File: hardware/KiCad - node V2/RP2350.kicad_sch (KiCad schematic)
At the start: 87 parts, among them J3 USB_C_Receptacle_USB2.0_14P, SW1 BOOTSEL, U1 RP2350A, U2 THVD1450D, U3 ADXL355BEZ, U4 TPS2121RUXR, U5 USBLC6-2SC6, U6 TLV75733PDBV, U7 W25Q128JVS, U8 TPS7A20xxxDBV

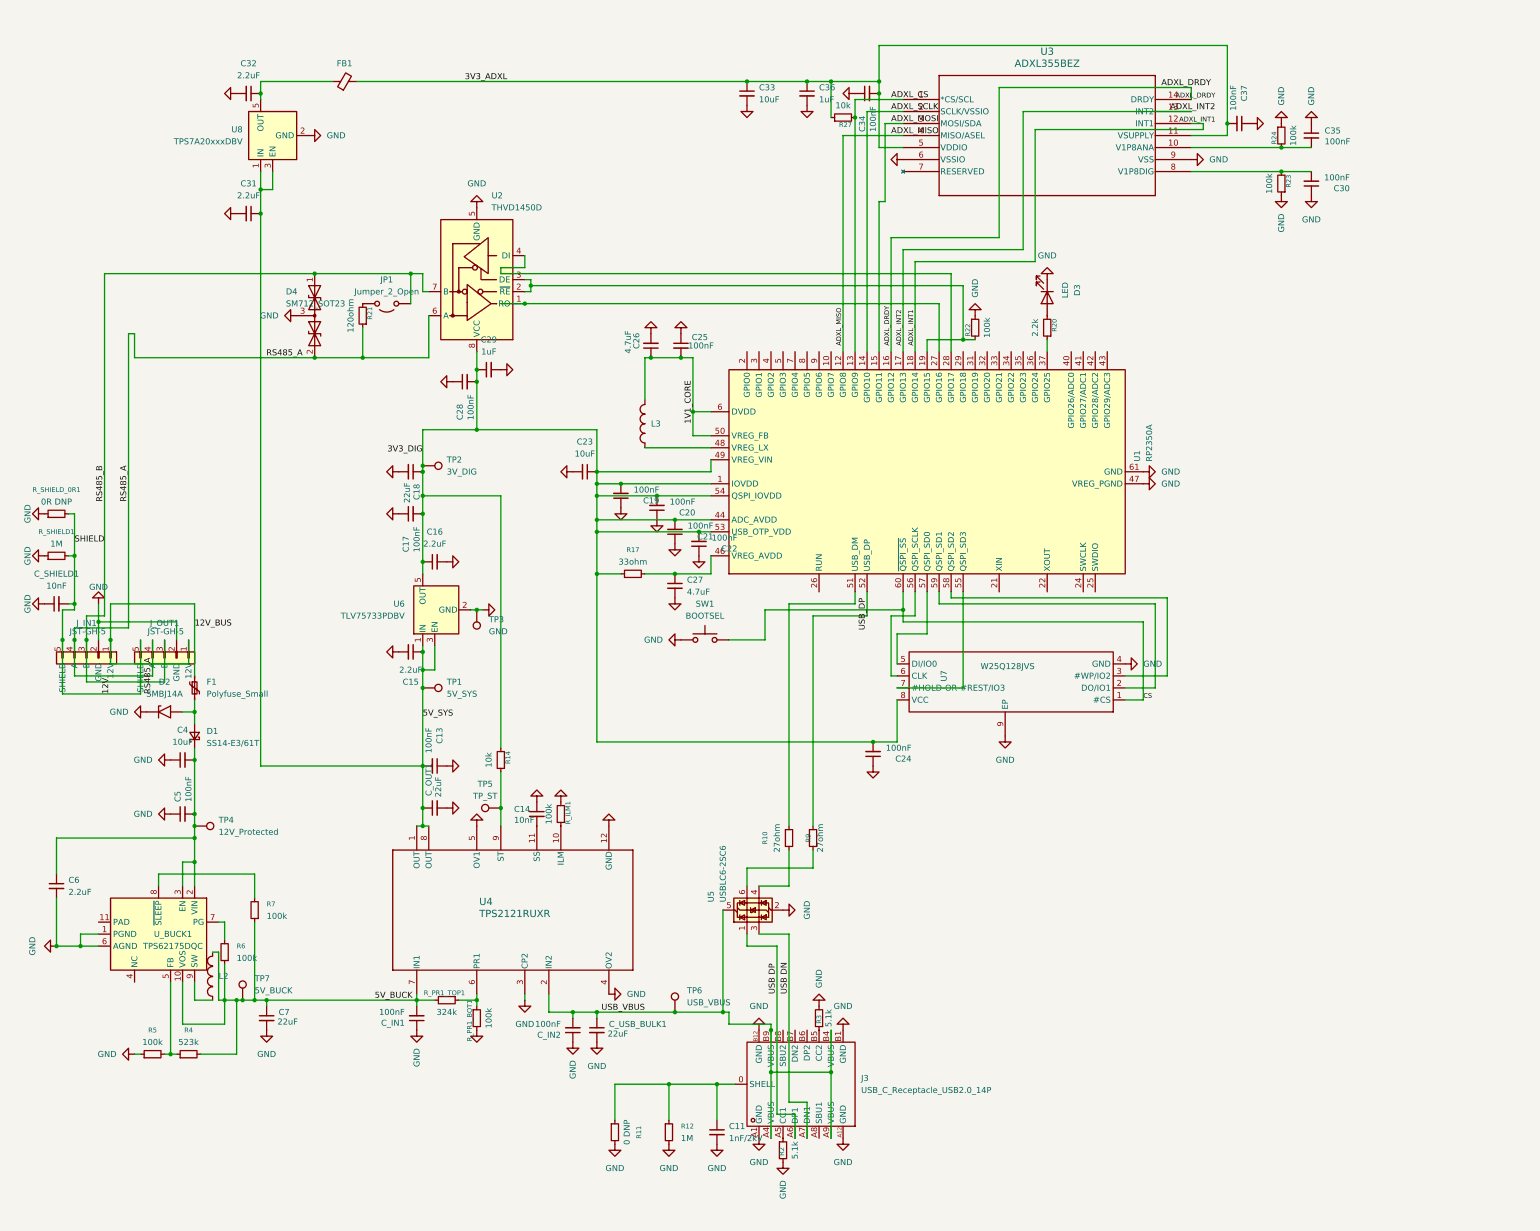
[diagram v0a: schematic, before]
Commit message: hardware: restored good schema with labels and pwr_flags
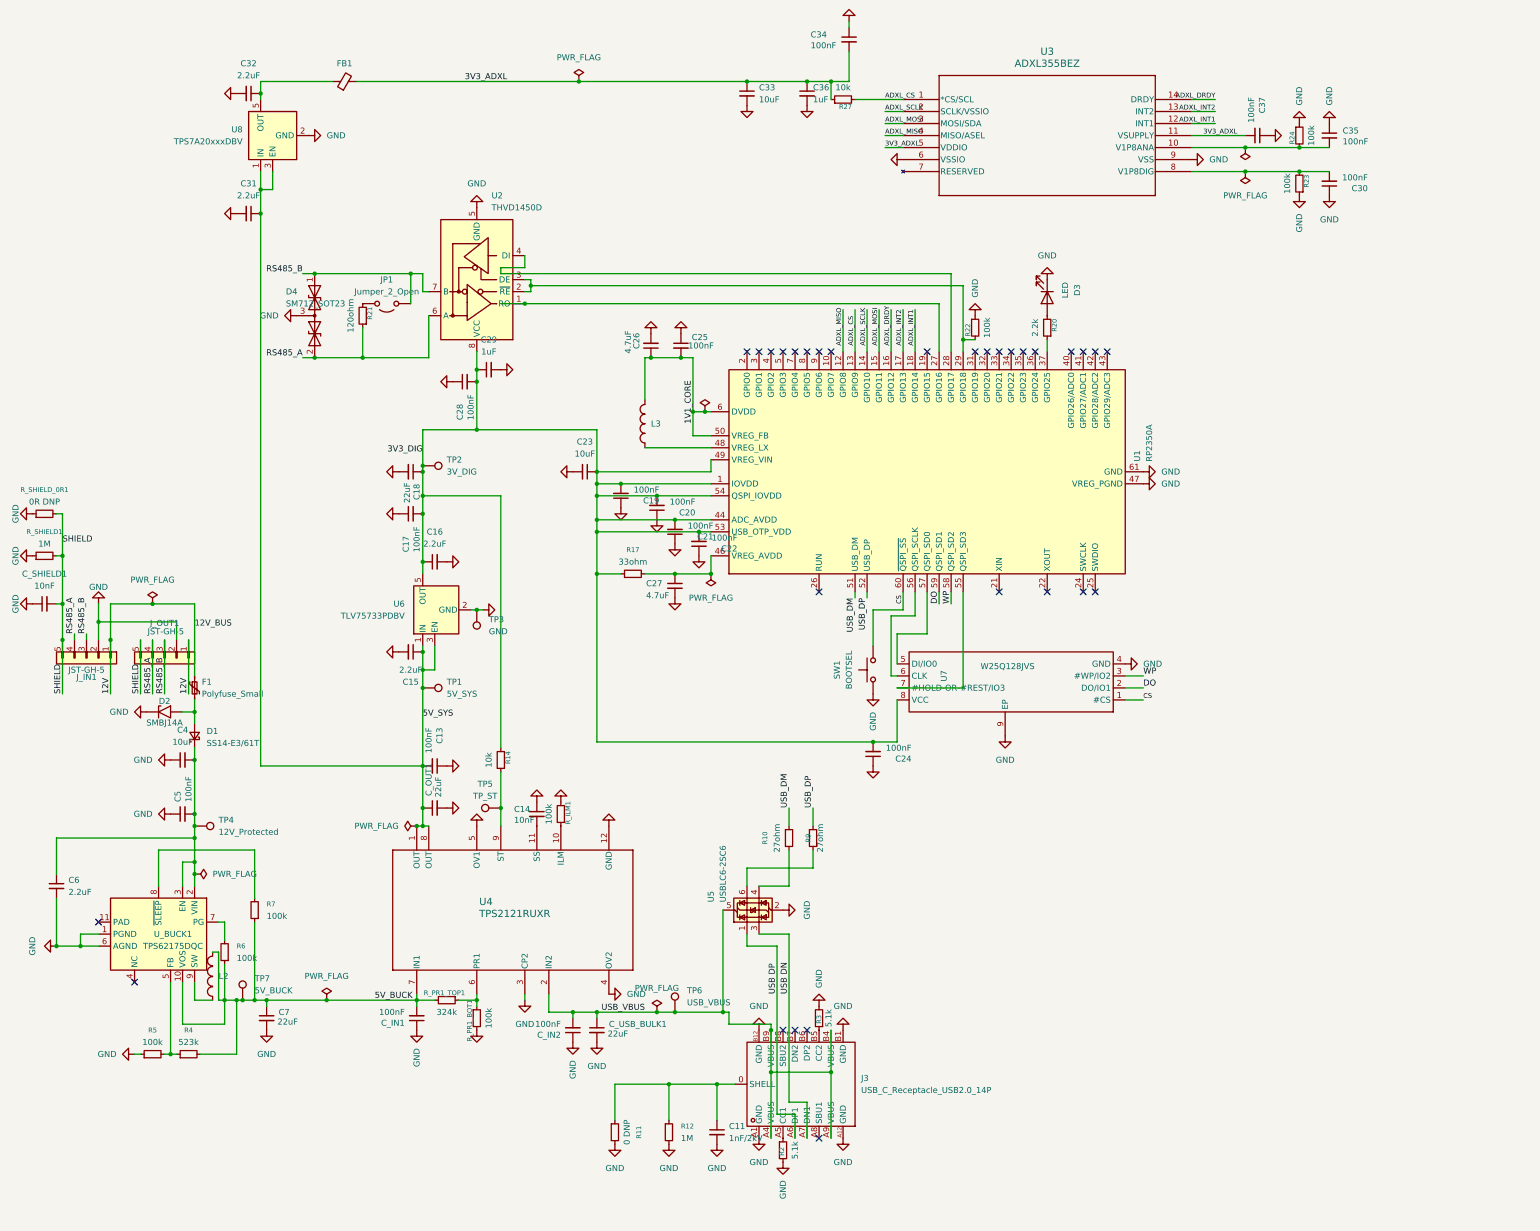
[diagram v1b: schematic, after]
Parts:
- U4: footprint footprints:TPS2121RUXR-VQFN-HR-12_L2.5-W2.0-P0.50-BL -> my_footprints:RUX0012A
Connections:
- net 12V_BUS is gone; now on net 12V: F1.1, J_IN1.1 (12V), J_OUT1.1 (12V)
- net 12V: no longer C_SHIELD1.2, J_IN1.5 (SHIELD), J_OUT1.5 (SHIELD), R_SHIELD1.2, R_SHIELD_0R1.2
- net at R22.2, U2.2 (~{RE}), U2.3 (DE): now also U1.29 (GPIO18); no longer U1.19 (GPIO15)
- net DO: now reaches U1.59 (QSPI_SD1), U7.2 (DO/IO1)
- net WP: now reaches U1.58 (QSPI_SD2), U7.3 (#WP/IO2)
- net USB_DM: now reaches R10.1, U1.51 (USB_DM)
- new net SHIELD: C_SHIELD1.2, J_IN1.5 (SHIELD), J_OUT1.5 (SHIELD), R_SHIELD1.2, R_SHIELD_0R1.2
- no-connect marks 0 -> 30
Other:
- moved on the sheet: C30, C34, C35, C37, C_SHIELD1, R23, R24, R27, R_SHIELD1, R_SHIELD_0R1, SW1

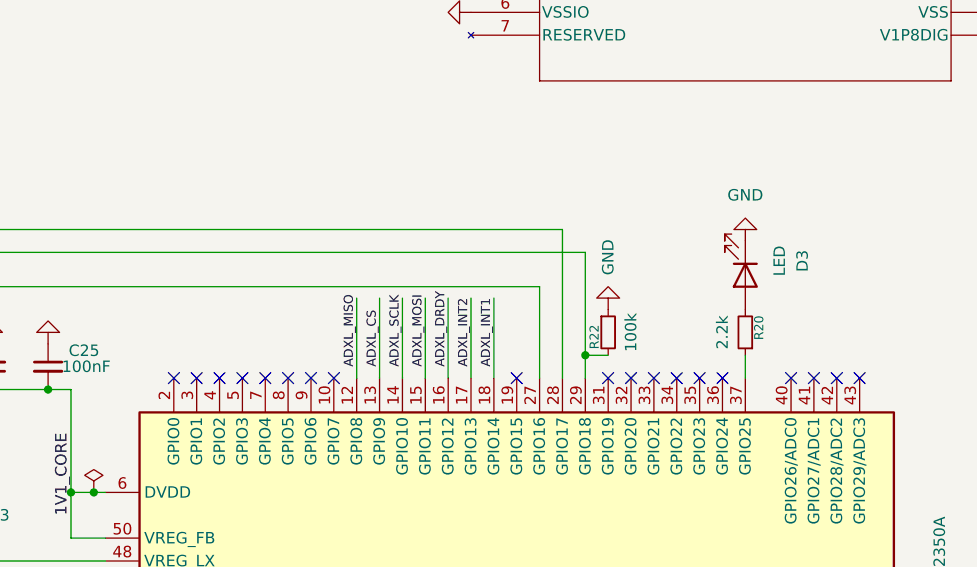
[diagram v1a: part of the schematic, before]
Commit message: hardware: pico pin change, moved mounting holes
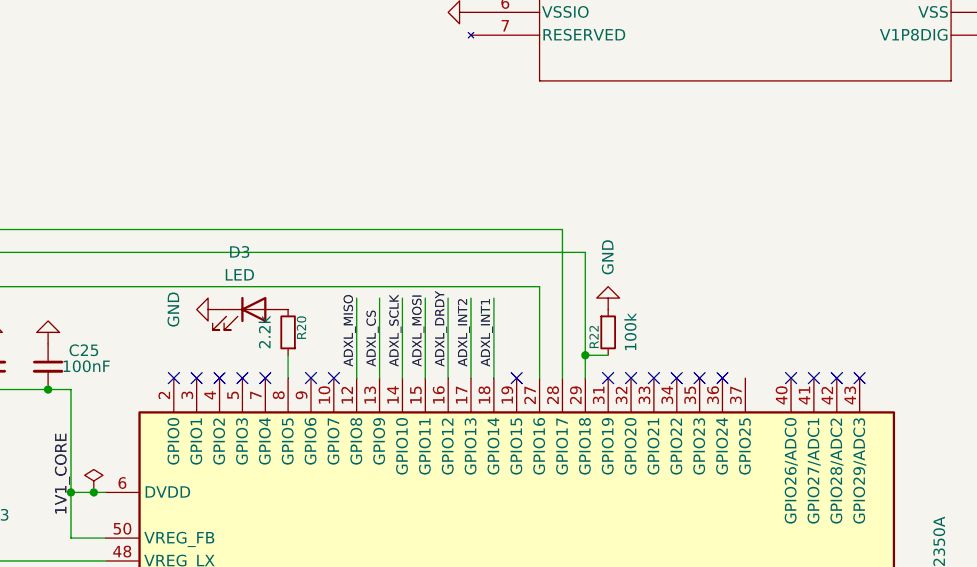
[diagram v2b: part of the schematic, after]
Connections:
- net at R20.1: now also U1.8 (GPIO5); no longer U1.37 (GPIO25)
- no-connect marks 30 -> 29
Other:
- moved on the sheet: D3, R20
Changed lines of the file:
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@@
 	)
 	(no_connect
-		(at 181.61 88.9)
-	)
-	(no_connect
 		(at 240.03 139.7)
 	)
@@
 	(wire
 		(pts
-			(xy 232.41 86.36) (xy 232.41 88.9)
-		)
-		(stroke
-			(width 0)
-			(type default)
-		)
-	)
-	(wire
-		(pts
 			(xy 142.24 116.84) (xy 161.29 116.84)
 		)
@@
 	(wire
 		(pts
+			(xy 181.61 86.36) (xy 181.61 88.9)
+		)
+		(stroke
+			(width 0)
+			(type default)
+		)
+	)
+	(wire
+		(pts
 			(xy 62.23 226.06) (xy 64.77 226.06)
 		)
@@
 	(symbol
 		(lib_id "power:GND")
-		(at 232.41 73.66 180)
+		(at 173.99 81.28 270)
 		(unit 1)
 		(body_style 1)
@@
 		(fields_autoplaced yes)
 		(property "Reference" "#PWR045"
-			(at 232.41 67.31 0)
+			(at 167.64 81.28 0)
 			(hide yes)
 			(show_name no)
@@
 		)
 		(property "Value" "GND"
-			(at 232.41 68.58 0)
+			(at 168.91 81.28 0)
 			(show_name no)
 			(do_not_autoplace no)
@@
 		)
 		(property "Footprint" ""
-			(at 232.41 73.66 0)
+			(at 173.99 81.28 0)
 			(hide yes)
 			(show_name no)
@@
 		)
 		(property "Datasheet" ""
-			(at 232.41 73.66 0)
+			(at 173.99 81.28 0)
 			(hide yes)
 			(show_name no)
@@
 		)
 		(property "Description" "Power symbol creates a global label with name \"GND\" , ground"
-			(at 232.41 73.66 0)
+			(at 173.99 81.28 0)
 			(hide yes)
 			(show_name no)
@@
 	(symbol
 		(lib_id "Device:R_Small")
-		(at 232.41 83.82 180)
+		(at 181.61 83.82 180)
 		(unit 1)
 		(body_style 1)
@@
 		(dnp no)
 		(property "Reference" "R20"
-			(at 233.934 83.312 90)
+			(at 183.134 83.312 90)
 			(show_name no)
 			(do_not_autoplace no)
@@
 		)
 		(property "Value" "2.2k"
-			(at 229.87 83.82 90)
+			(at 179.07 83.82 90)
 			(show_name no)
 			(do_not_autoplace no)
@@
 		)
 		(property "Footprint" "Resistor_SMD:R_0603_1608Metric"
-			(at 232.41 83.82 0)
+			(at 181.61 83.82 0)
 			(hide yes)
 			(show_name no)
@@
 		)
 		(property "Datasheet" ""
-			(at 232.41 83.82 0)
+			(at 181.61 83.82 0)
 			(hide yes)
 			(show_name no)
@@
 		)
 		(property "Description" "Resistor, small symbol"
-			(at 232.41 83.82 0)
+			(at 181.61 83.82 0)
 			(hide yes)
 			(show_name no)
@@
 	(symbol
 		(lib_id "Device:LED")
-		(at 232.41 77.47 270)
+		(at 177.8 81.28 0)
 		(unit 1)
 		(body_style 1)
@@
 		(fields_autoplaced yes)
 		(property "Reference" "D3"
-			(at 238.76 75.8825 0)
+			(at 176.2125 74.93 0)
 			(show_name no)
 			(do_not_autoplace no)
@@
 		)
 		(property "Value" "LED"
-			(at 236.22 75.8825 0)
+			(at 176.2125 77.47 0)
 			(show_name no)
 			(do_not_autoplace no)
@@
 		)
 		(property "Footprint" "LED_SMD:LED_0603_1608Metric"
-			(at 232.41 77.47 0)
+			(at 177.8 81.28 0)
 			(hide yes)
 			(show_name no)
@@
 		)
 		(property "Datasheet" ""
-			(at 232.41 77.47 0)
+			(at 177.8 81.28 0)
 			(hide yes)
 			(show_name no)
@@
 		)
 		(property "Description" "Light emitting diode"
-			(at 232.41 77.47 0)
+			(at 177.8 81.28 0)
 			(hide yes)
 			(show_name no)
@@
 		)
 		(property "Sim.Pins" "1=K 2=A"
-			(at 232.41 77.47 0)
+			(at 177.8 81.28 0)
 			(hide yes)
 			(show_name no)
